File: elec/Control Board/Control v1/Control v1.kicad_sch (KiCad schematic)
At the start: 45 parts, among them J1 DB9_Female_MountingHoles, J10 Conn_02x12_Odd_Even, J11 Screw_Terminal_01x02, J14 Conn_01x08, J2 Conn_01x08, J3 Conn_01x08, J4 Conn_01x08, J5 Conn_01x08, J6 Conn_01x08, J7 Conn_02x18_Odd_Even, J8 Conn_01x10, J9 Conn_01x10

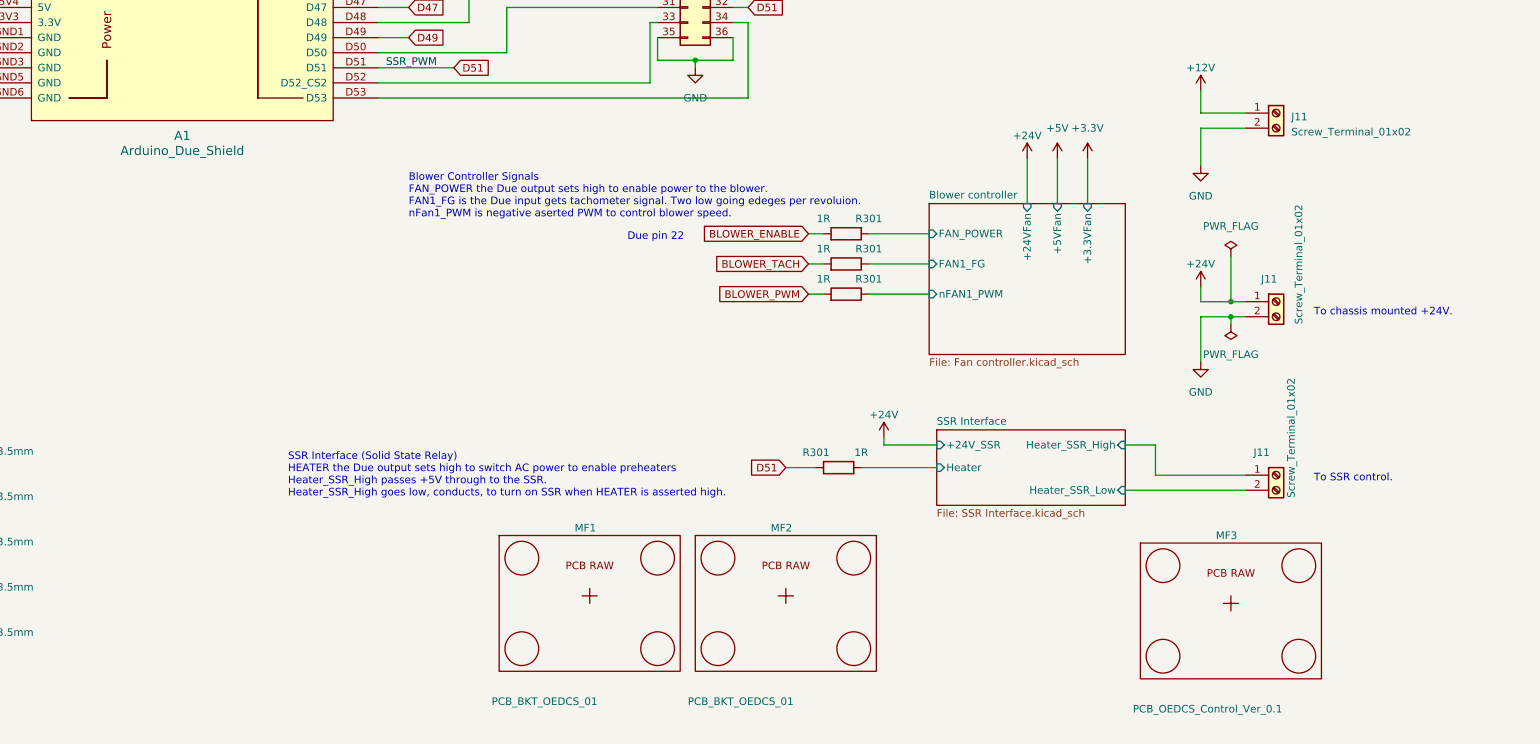
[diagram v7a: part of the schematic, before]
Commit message: Add header sockets. Refine PCB placement, temprature sensors.
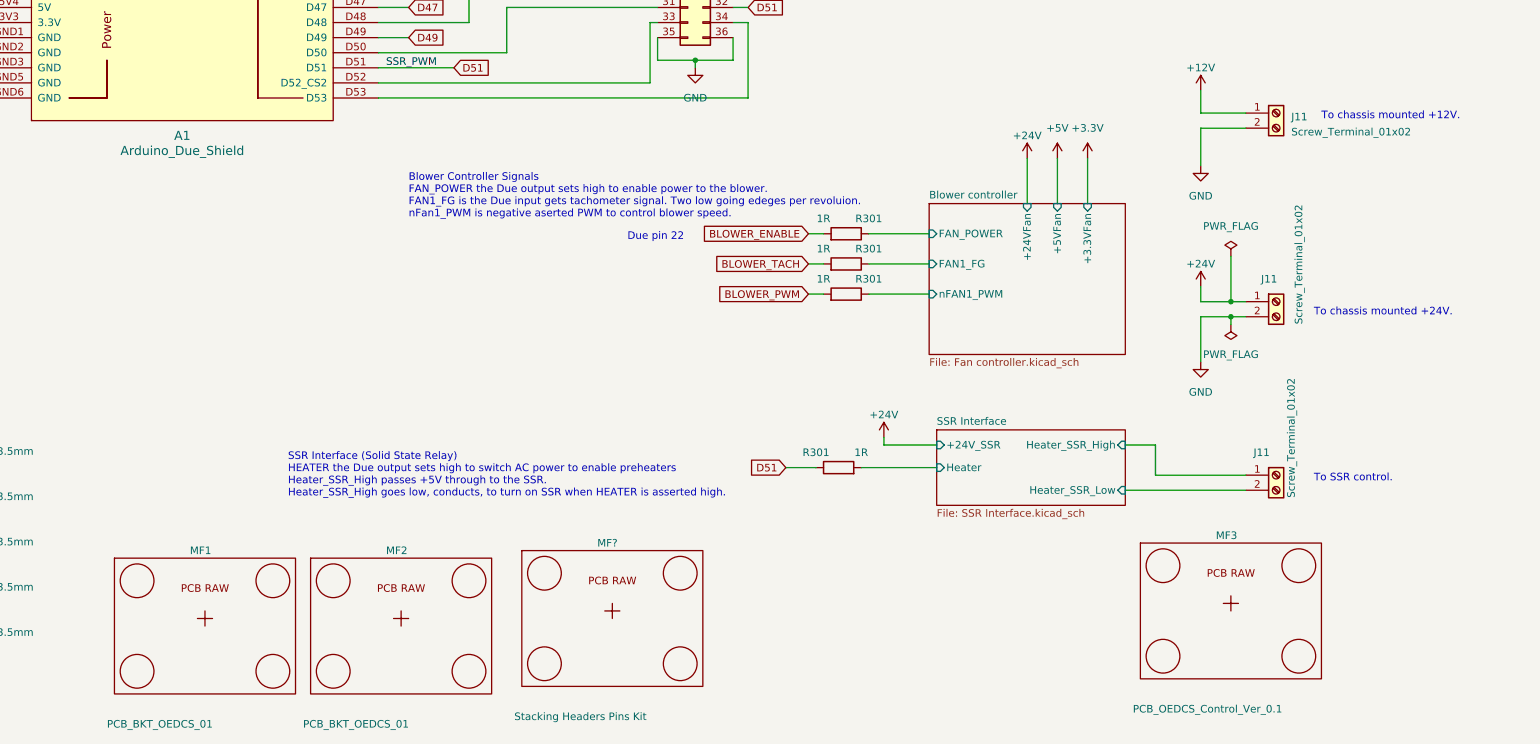
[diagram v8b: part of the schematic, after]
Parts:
- added MF?: Stacking Headers Pins Kit, NA, symbol GPAD_SCH_LIB:PCB_GPAD_VER1
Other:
- note added: "To chassis mounted +12V."
- moved on the sheet: MF1, MF2
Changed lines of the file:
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@@
     (effects (font (size 1.27 1.27)) (justify left bottom))
   )
+  (text "To chassis mounted +12V." (at 402.59 175.26 0)
+    (effects (font (size 1.27 1.27)) (justify left bottom))
+  )
   (text "Blower Controller Signals\nFAN_POWER the Due output sets high to enable power to the blower.\nFAN1_FG is the Due input gets tachometer signal. Two low going edeges per revoluion.\nnFan1_PWM is negative aserted PWM to control blower speed."
     (at 248.92 191.77 0)
@@
     )
   )
-  (symbol (lib_id "GPAD_SCH_LIB:PCB_GPAD_VER1") (at 279.4 255.27 0) (unit 1)
+  (symbol (lib_id "GPAD_SCH_LIB:PCB_GPAD_VER1") (at 214.63 259.08 0) (unit 1)
     (in_bom yes) (on_board no) (dnp no)
-    (property "Reference" "MF1" (at 276.86 243.84 0)
+    (property "Reference" "MF1" (at 212.09 247.65 0)
       (effects (font (size 1.27 1.27)) (justify left))
     )
-    (property "Value" "PCB_BKT_OEDCS_01" (at 262.89 273.05 0)
+    (property "Value" "PCB_BKT_OEDCS_01" (at 198.12 276.86 0)
       (effects (font (size 1.27 1.27)) (justify left))
     )
-    (property "Footprint" "NA" (at 279.4 255.27 0)
+    (property "Footprint" "NA" (at 214.63 259.08 0)
       (effects (font (size 1.27 1.27)) hide)
     )
-    (property "Datasheet" "PCB_BKT_OEDCS_01" (at 279.4 255.27 0)
+    (property "Datasheet" "PCB_BKT_OEDCS_01" (at 214.63 259.08 0)
       (effects (font (size 0 0)) hide)
     )
-    (property "Distributor 1" "PublicInvention" (at 279.4 255.27 0)
+    (property "Distributor 1" "PublicInvention" (at 214.63 259.08 0)
       (effects (font (size 1.27 1.27)) hide)
     )
-    (property "Distributor 1 PN" "PCB_BKT_OEDCS_01" (at 279.4 255.27 0)
+    (property "Distributor 1 PN" "PCB_BKT_OEDCS_01" (at 214.63 259.08 0)
       (effects (font (size 0 0)) hide)
     )
-    (property "Cost" "1000000" (at 279.4 255.27 0)
+    (property "Cost" "1000000" (at 214.63 259.08 0)
       (effects (font (size 1.27 1.27)) hide)
     )
-    (property "AssemblyType" "HAND" (at 279.4 255.27 0)
+    (property "AssemblyType" "HAND" (at 214.63 259.08 0)
       (effects (font (size 1.27 1.27)) hide)
     )
-    (property "Description" "PCB_BKT_OEDCS_01" (at 279.4 255.27 0)
+    (property "Description" "PCB_BKT_OEDCS_01" (at 214.63 259.08 0)
       (effects (font (size 1.27 1.27)) hide)
     )
-    (property "MPN" "PCB_BKT_OEDCS_01" (at 279.4 255.27 0)
+    (property "MPN" "PCB_BKT_OEDCS_01" (at 214.63 259.08 0)
       (effects (font (size 1.27 1.27)) hide)
     )
-    (property "LongLead" "YES" (at 279.4 255.27 0)
+    (property "LongLead" "YES" (at 214.63 259.08 0)
       (effects (font (size 1.27 1.27)) hide)
     )
-    (property "Manufacturer" "PublicInvention" (at 279.4 255.27 0)
+    (property "Manufacturer" "PublicInvention" (at 214.63 259.08 0)
       (effects (font (size 1.27 1.27)) hide)
     )
@@
     )
   )
+  (symbol (lib_id "GPAD_SCH_LIB:PCB_GPAD_VER1") (at 283.21 257.81 0) (unit 1)
+    (in_bom yes) (on_board no) (dnp no)
+    (property "Reference" "MF?" (at 280.67 246.38 0)
+      (effects (font (size 1.27 1.27)) (justify left))
+    )
+    (property "Value" "Stacking Headers Pins Kit" (at 266.7 275.59 0)
+      (effects (font (size 1.27 1.27)) (justify left))
+    )
+    (property "Footprint" "NA" (at 283.21 257.81 0)
+      (effects (font (size 1.27 1.27)) hide)
+    )
+    (property "Datasheet" "https://www.amazon.com/Treedix-Stacking-Headers-Stackable-Compatible/dp/B08G4FGBPQ/ref=sr_1_6" (at 283.21 257.81 0)
+      (effects (font (size 0 0)) hide)
+    )
+    (property "Distributor 1" "Amazon" (at 283.21 257.81 0)
+      (effects (font (size 1.27 1.27)) hide)
+    )
+    (property "Distributor 1 PN" "https://www.amazon.com/Treedix-Stacking-Headers-Stackable-Compatible/dp/B08G4FGBPQ/ref=sr_1_6" (at 283.21 257.81 0)
+      (effects (font (size 0 0)) hide)
+    )
+    (property "Cost" "4.50" (at 283.21 257.81 0)
+      (effects (font (size 1.27 1.27)) hide)
+    )
+    (property "AssemblyType" "HAND" (at 283.21 257.81 0)
+      (effects (font (size 1.27 1.27)) hide)
+    )
+    (property "Description" "Stacking Headers Pins Kit Stackable Female Headers Compatible with Arduino Mega 2560(28pcs in Total)" (at 283.21 257.81 0)
+      (effects (font (size 1.27 1.27)) hide)
+    )
+    (property "MPN" "PCB_BKT_OEDCS_01" (at 283.21 257.81 0)
+      (effects (font (size 1.27 1.27)) hide)
+    )
+    (property "LongLead" "YES" (at 283.21 257.81 0)
+      (effects (font (size 1.27 1.27)) hide)
+    )
+    (property "Manufacturer" "TreeDix" (at 283.21 257.81 0)
+      (effects (font (size 1.27 1.27)) hide)
+    )
+    (instances
+      (project "Control v1"
+        (path "/c68c9deb-8d4d-42f0-adf8-4d3022f4ee59"
+          (reference "MF?") (unit 1)
+        )
+      )
+    )
+  )
   (symbol (lib_id "Connector_Generic:Conn_01x08") (at 132.08 161.29 0) (mirror y) (unit 1)
     (in_bom yes) (on_board yes) (dnp no)
@@
     )
   )
-  (symbol (lib_id "GPAD_SCH_LIB:PCB_GPAD_VER1") (at 312.42 255.27 0) (unit 1)
+  (symbol (lib_id "GPAD_SCH_LIB:PCB_GPAD_VER1") (at 247.65 259.08 0) (unit 1)
     (in_bom yes) (on_board no) (dnp no)
-    (property "Reference" "MF2" (at 309.88 243.84 0)
+    (property "Reference" "MF2" (at 245.11 247.65 0)
       (effects (font (size 1.27 1.27)) (justify left))
     )
-    (property "Value" "PCB_BKT_OEDCS_01" (at 295.91 273.05 0)
+    (property "Value" "PCB_BKT_OEDCS_01" (at 231.14 276.86 0)
       (effects (font (size 1.27 1.27)) (justify left))
     )
-    (property "Footprint" "NA" (at 312.42 255.27 0)
+    (property "Footprint" "NA" (at 247.65 259.08 0)
       (effects (font (size 1.27 1.27)) hide)
     )
-    (property "Datasheet" "PCB_BKT_OEDCS_01" (at 312.42 255.27 0)
+    (property "Datasheet" "PCB_BKT_OEDCS_01" (at 247.65 259.08 0)
       (effects (font (size 0 0)) hide)
     )
-    (property "Distributor 1" "PublicInvention" (at 312.42 255.27 0)
+    (property "Distributor 1" "PublicInvention" (at 247.65 259.08 0)
       (effects (font (size 1.27 1.27)) hide)
     )
-    (property "Distributor 1 PN" "PCB_BKT_OEDCS_01" (at 312.42 255.27 0)
+    (property "Distributor 1 PN" "PCB_BKT_OEDCS_01" (at 247.65 259.08 0)
       (effects (font (size 0 0)) hide)
     )
-    (property "Cost" "1000000" (at 312.42 255.27 0)
+    (property "Cost" "1000000" (at 247.65 259.08 0)
       (effects (font (size 1.27 1.27)) hide)
     )
-    (property "AssemblyType" "HAND" (at 312.42 255.27 0)
+    (property "AssemblyType" "HAND" (at 247.65 259.08 0)
       (effects (font (size 1.27 1.27)) hide)
     )
-    (property "Description" "PCB_BKT_OEDCS_01" (at 312.42 255.27 0)
+    (property "Description" "PCB_BKT_OEDCS_01" (at 247.65 259.08 0)
       (effects (font (size 1.27 1.27)) hide)
     )
-    (property "MPN" "PCB_BKT_OEDCS_01" (at 312.42 255.27 0)
+    (property "MPN" "PCB_BKT_OEDCS_01" (at 247.65 259.08 0)
       (effects (font (size 1.27 1.27)) hide)
     )
-    (property "LongLead" "YES" (at 312.42 255.27 0)
+    (property "LongLead" "YES" (at 247.65 259.08 0)
       (effects (font (size 1.27 1.27)) hide)
     )
-    (property "Manufacturer" "PublicInvention" (at 312.42 255.27 0)
+    (property "Manufacturer" "PublicInvention" (at 247.65 259.08 0)
       (effects (font (size 1.27 1.27)) hide)
     )
